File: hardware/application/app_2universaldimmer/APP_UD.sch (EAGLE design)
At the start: 94 parts, among them IC102 LM324N, IC2 LM324N, Q1 IRFP460, Q101 IRFP460, Q102 IRFP460, Q103 BC546B, Q104 MPSA44, Q2 IRFP460, Q3 BC546B, Q4 MPSA44

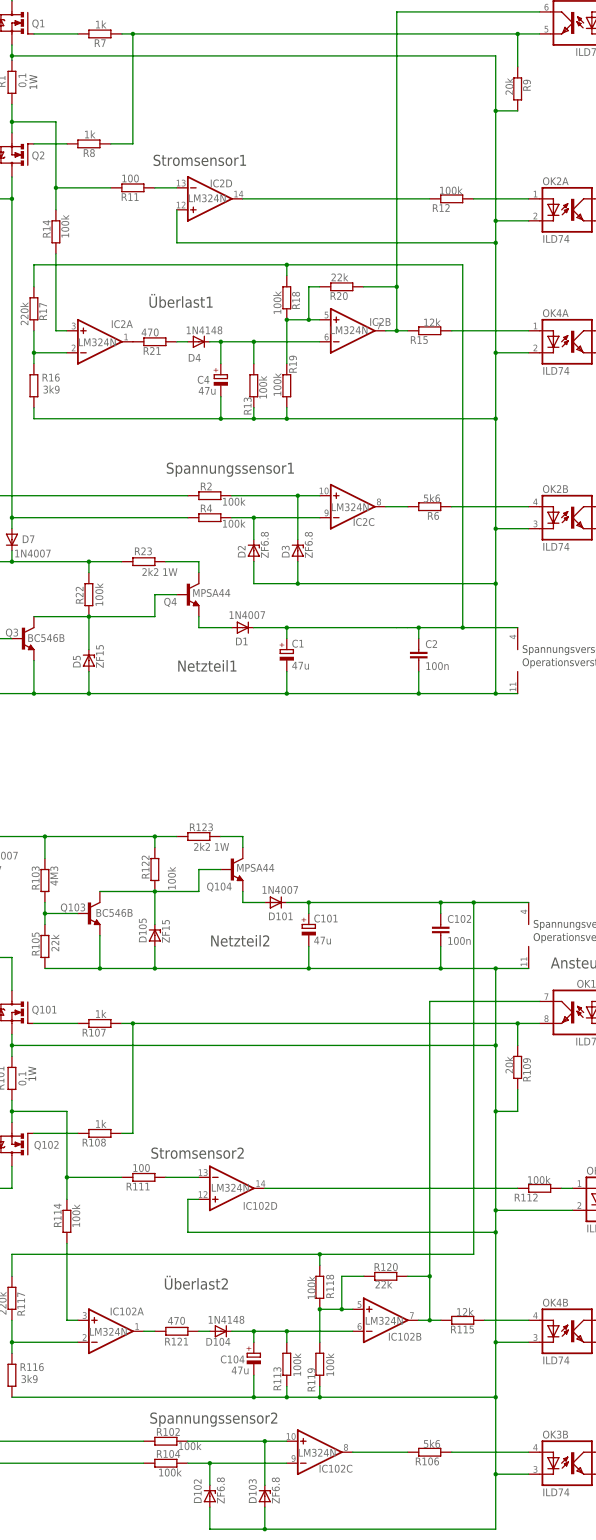
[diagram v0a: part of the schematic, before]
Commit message: Universaldimmer: V2.4  R23 nun 5Watt,deshalb Layout geändert, Schaltung ist gleich BOM und Warenkorb hinzugefügt
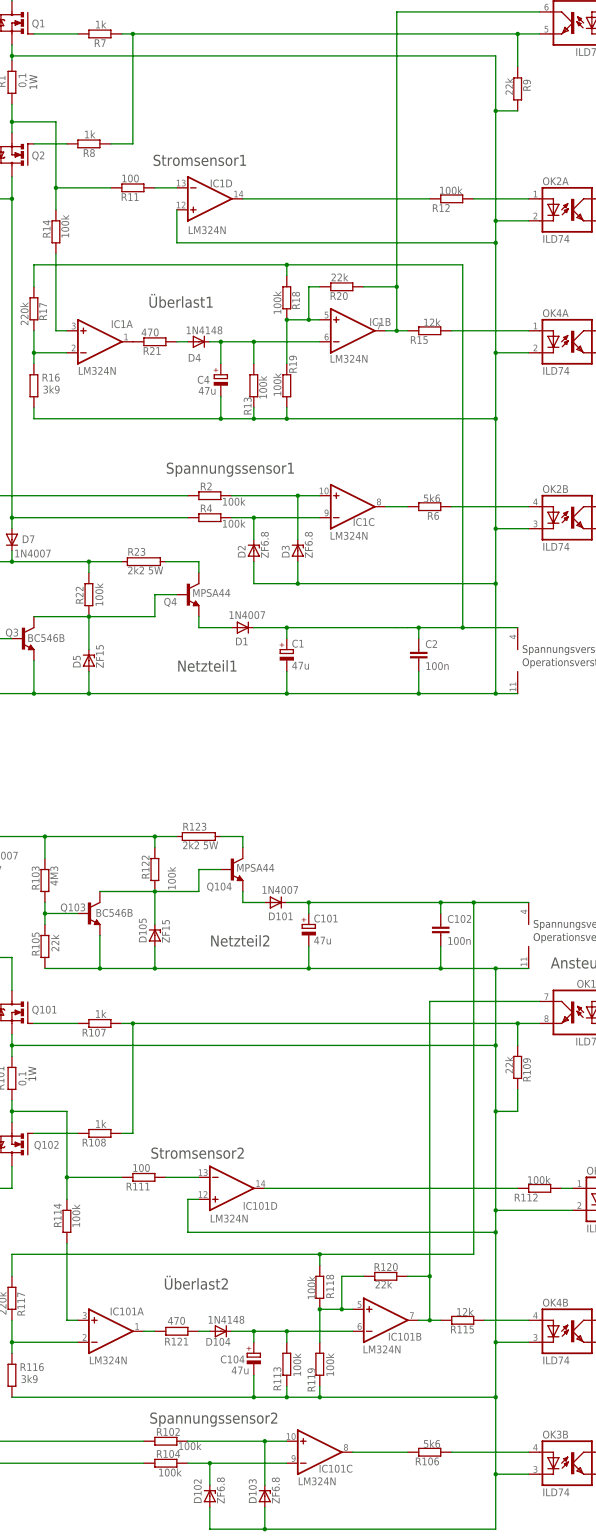
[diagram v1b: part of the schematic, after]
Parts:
- R109, R9: value 20k -> 22k
- R112: device rcl:R-EU_0207/15 -> rcl:R-EU_0207/12
- R123, R23: value 2k2 1W -> 2k2 5W; device rcl:R-EU_0207/15 -> resistor-power:R
- renumbered IC102 to IC101, IC2 to IC1
